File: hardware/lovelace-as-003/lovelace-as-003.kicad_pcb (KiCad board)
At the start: 4 copper layers, 37 x 41 mm, 65 parts, among them J1 HRO TYPE-C-31-M-12, J2 PJ-320D, SW1 B3U-1000P, U1 ESP32-WROVER-E-N8R8, U2 PCM5102APWR, U3 TPS62162DSGR, U4 TPS7A2033PDBVR, U5 USBLC6-2SC6, U6 TPS259470ARPWR, U7 CH340N

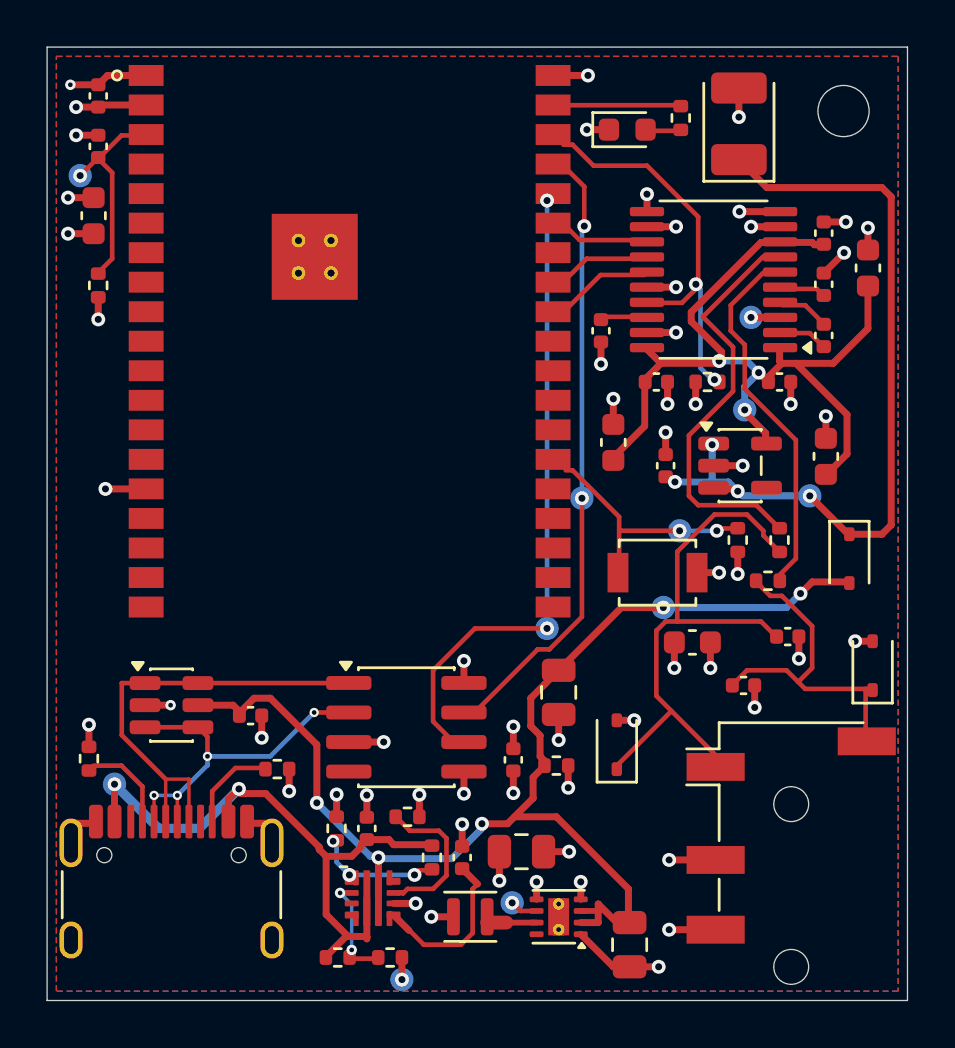
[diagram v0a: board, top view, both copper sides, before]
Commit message: Review AS-003 before ordering and keep vias off top SMD pads
- pinout_check.py: netlist against a pin table written from the vendor
  datasheets (138 checks), run by make_board.sh after placement
- sim/power_path.py: ngspice behavioural model of the power path (eFuse
  start-up, ESP32 pulsed load, C25 hold-up on unplug)
- Router passes that place vias use --same-net-pad-clearance 0.1; OVLO and
  ILIM at the eFuse QFN are drawn in build_pcb.py; test-pad vias stay off
  top pads; audio copper is locked after its pass so later passes cannot
  move DAC_L/R onto B.Cu
- audit_pcb.py fails on any via touching a top SMD pad (was 10, now 0)
- REVIEW_NETLIST.md, REVIEW_LAYOUT.md, BRINGUP.md: findings, simulation
  results, no-scope eFuse check, JLC edge rails, USB ground noise test
- Silkscreen editor updates and regenerated release, reports and renders

Co-Authored-By: Claude Opus 5.5 <noreply@anthropic.com>
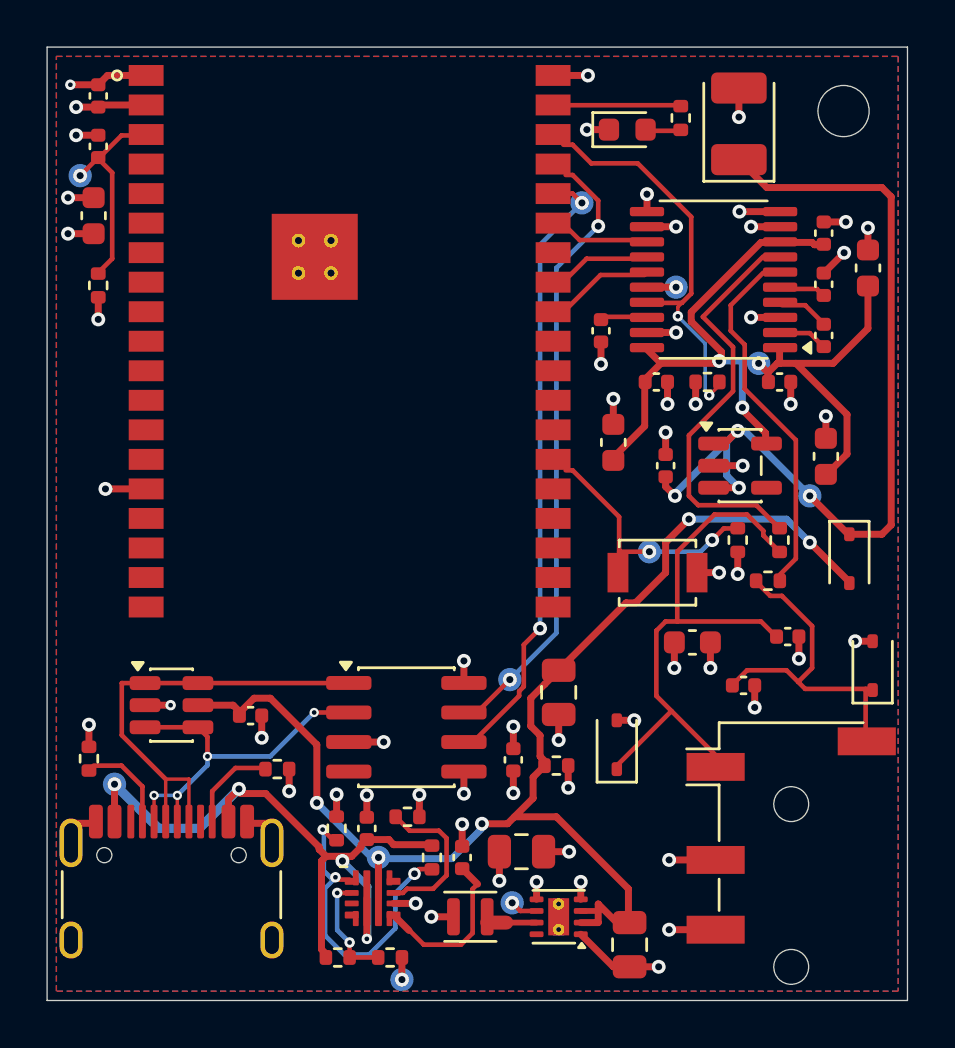
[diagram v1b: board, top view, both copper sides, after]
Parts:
- moved RX 18.4 mm to (23.0, 6.70)
- moved 5V 16.3 mm to (14.2, 34.9)
- moved TX 8.39 mm to (19.9, 27.2)
- moved GND2 3.48 mm to (27.0, 10.3)
- moved 3V3A 2.09 mm to (30.6, 13.6)
- moved IO0 1.58 mm to (25.9, 21.7)
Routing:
- net POWER_EN: track 5.26 -> 13.3 mm
- net +5V_DAC: track 34.2 -> 38.3 mm
- net +5V: track 53.0 -> 56.0 mm
- net VBUS: track 26.2 -> 28.5 mm, vias 2 -> 4
- net UART_RX: track 27.5 -> 26.5 mm
- net OVLO: track 4.06 -> 4.85 mm
- net XSMT: track 16.6 -> 17.4 mm
- net BOOT: track 10.5 -> 11.0 mm
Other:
- board text added: "4.75-5.25V / PD OK ACTIVE SPEAKER / AMP PLUG THEN PWR HOLD 3s: BT PAIR HOLD + USB: FLASH"
- board text added: "LOVELACE AS-003 rev A Airplay 2 / Spotify / BT"
- board text added: "lovelace-research.com @lovelaceresearch"
- board text removed: "AS-003 rev A Wi-Fi + BT"
- board text removed: "AUX"
- board text removed: "BUTTON"
- board text removed: "LOVELACE"
- board text removed: "USB-C 5V"
